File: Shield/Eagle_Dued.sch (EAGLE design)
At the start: 114 parts, among them IC1 7805TV, IC2 LM340MP-05, J10 Analog Inputs, J11 MOSFET OUTPUTS, J12 CANBUS, J8 DIGITAL INPUTS, X1 87758-1216

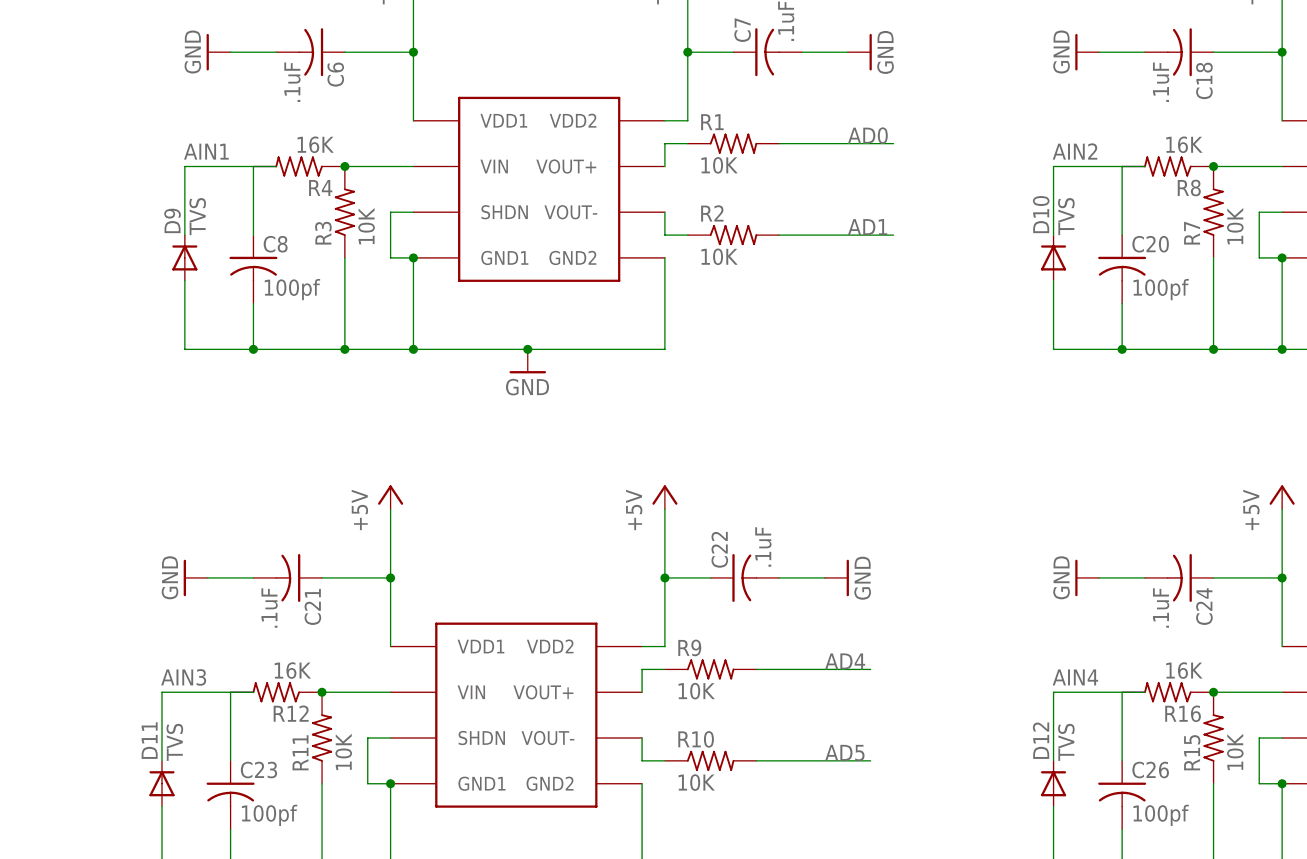
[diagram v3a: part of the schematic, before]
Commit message: Fixed a couple of errors in the schematic
Placed all parts on board approximately where they'll end up
(in theory)
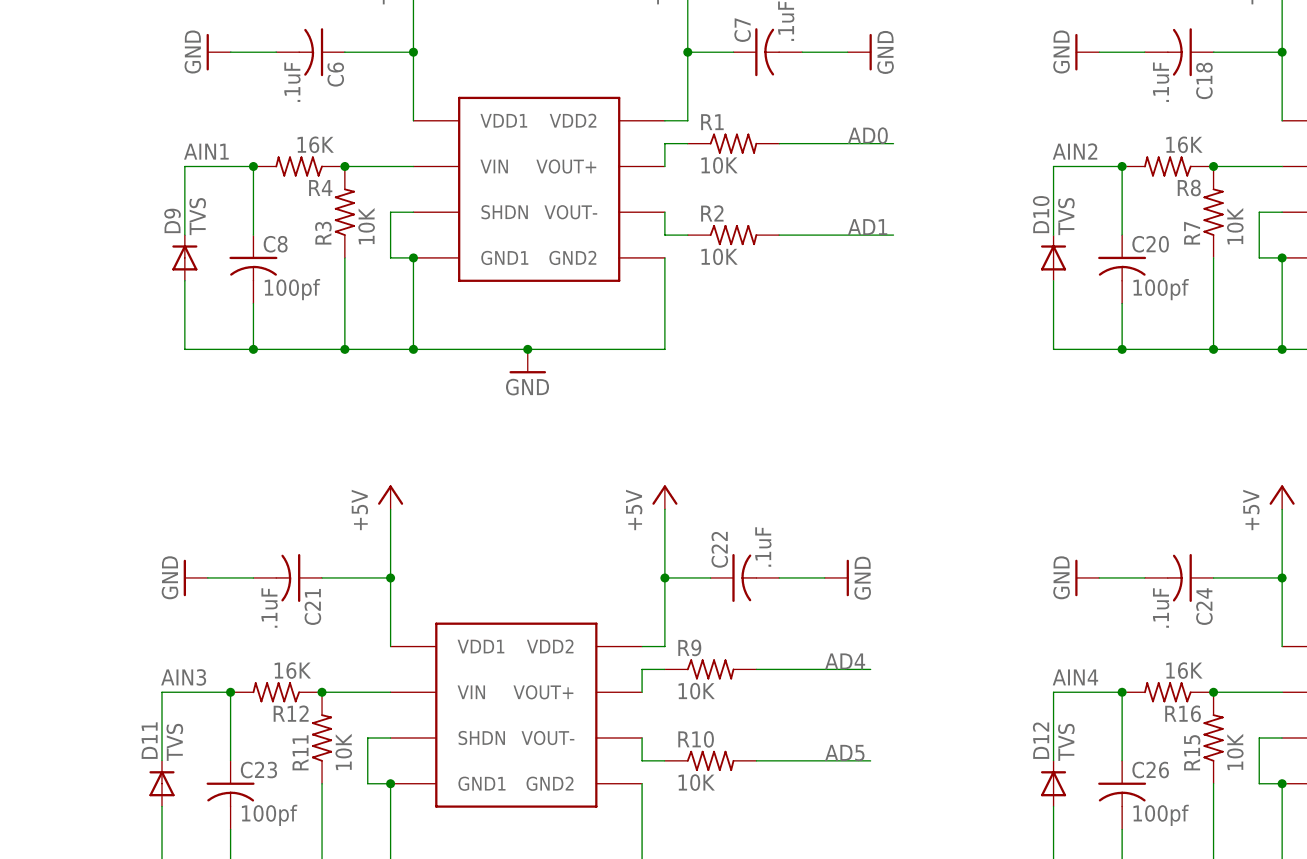
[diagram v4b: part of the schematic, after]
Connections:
- removed net N$14: C20.1, R8.2
- removed net N$18: C23.1, R12.2
- removed net N$22: C26.1, R16.2
- removed net N$9: C8.1, R4.2
- net AIN1: now also C8.1, R4.2
- net AIN2: now also C20.1, R8.2
- net AIN3: now also C23.1, R12.2
- net AIN4: now also C26.1, R16.2
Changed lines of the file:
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@@
 </segment>
 </net>
-<net name="N$9" class="0">
-<segment>
+<net name="AIN4" class="0">
+<segment>
+<pinref part="J10" gate="G$1" pin="4"/>
+<wire x1="398.78" y1="83.82" x2="411.48" y2="83.82" width="0.1524" layer="91"/>
+<label x="403.86" y="83.82" size="1.778" layer="95"/>
+</segment>
+<segment>
+<pinref part="D12" gate="G$1" pin="C"/>
+<wire x1="424.18" y1="-175.26" x2="424.18" y2="-182.88" width="0.1524" layer="91"/>
+<label x="429.26" y="-172.72" size="1.778" layer="95" rot="R180"/>
+<pinref part="R16" gate="G$1" pin="2"/>
+<pinref part="C26" gate="G$1" pin="1"/>
+<wire x1="431.8" y1="-175.26" x2="431.8" y2="-182.88" width="0.1524" layer="91"/>
+<wire x1="424.18" y1="-175.26" x2="431.8" y2="-175.26" width="0.1524" layer="91"/>
+<junction x="431.8" y="-175.26"/>
+</segment>
+</net>
+<net name="AIN3" class="0">
+<segment>
+<pinref part="J10" gate="G$1" pin="3"/>
+<wire x1="398.78" y1="81.28" x2="411.48" y2="81.28" width="0.1524" layer="91"/>
+<label x="403.86" y="81.28" size="1.778" layer="95"/>
+</segment>
+<segment>
+<pinref part="D11" gate="G$1" pin="C"/>
+<wire x1="325.12" y1="-175.26" x2="325.12" y2="-182.88" width="0.1524" layer="91"/>
+<label x="330.2" y="-172.72" size="1.778" layer="95" rot="R180"/>
+<pinref part="R12" gate="G$1" pin="2"/>
+<pinref part="C23" gate="G$1" pin="1"/>
+<wire x1="332.74" y1="-175.26" x2="332.74" y2="-182.88" width="0.1524" layer="91"/>
+<wire x1="325.12" y1="-175.26" x2="332.74" y2="-175.26" width="0.1524" layer="91"/>
+<junction x="332.74" y="-175.26"/>
+</segment>
+</net>
+<net name="AIN2" class="0">
+<segment>
+<pinref part="J10" gate="G$1" pin="2"/>
+<wire x1="398.78" y1="78.74" x2="411.48" y2="78.74" width="0.1524" layer="91"/>
+<label x="403.86" y="78.74" size="1.778" layer="95"/>
+</segment>
+<segment>
+<pinref part="D10" gate="G$1" pin="C"/>
+<wire x1="424.18" y1="-116.84" x2="424.18" y2="-124.46" width="0.1524" layer="91"/>
+<label x="429.26" y="-114.3" size="1.778" layer="95" rot="R180"/>
+<pinref part="R8" gate="G$1" pin="2"/>
+<pinref part="C20" gate="G$1" pin="1"/>
+<wire x1="431.8" y1="-116.84" x2="431.8" y2="-124.46" width="0.1524" layer="91"/>
+<wire x1="424.18" y1="-116.84" x2="431.8" y2="-116.84" width="0.1524" layer="91"/>
+<junction x="431.8" y="-116.84"/>
+</segment>
+</net>
+<net name="AIN1" class="0">
+<segment>
+<pinref part="J10" gate="G$1" pin="1"/>
+<wire x1="398.78" y1="76.2" x2="411.48" y2="76.2" width="0.1524" layer="91"/>
+<label x="403.86" y="76.2" size="1.778" layer="95"/>
+</segment>
+<segment>
+<pinref part="D9" gate="G$1" pin="C"/>
+<wire x1="327.66" y1="-116.84" x2="327.66" y2="-124.46" width="0.1524" layer="91"/>
+<label x="332.74" y="-114.3" size="1.778" layer="95" rot="R180"/>
 <pinref part="R4" gate="G$1" pin="2"/>
 <pinref part="C8" gate="G$1" pin="1"/>
 <wire x1="335.28" y1="-116.84" x2="335.28" y2="-124.46" width="0.1524" layer="91"/>
-</segment>
-</net>
-<net name="AIN4" class="0">
-<segment>
-<pinref part="J10" gate="G$1" pin="4"/>
-<wire x1="398.78" y1="83.82" x2="411.48" y2="83.82" width="0.1524" layer="91"/>
-<label x="403.86" y="83.82" size="1.778" layer="95"/>
-</segment>
-<segment>
-<wire x1="434.34" y1="-175.26" x2="424.18" y2="-175.26" width="0.1524" layer="91"/>
-<pinref part="D12" gate="G$1" pin="C"/>
-<wire x1="424.18" y1="-175.26" x2="424.18" y2="-182.88" width="0.1524" layer="91"/>
-<label x="429.26" y="-172.72" size="1.778" layer="95" rot="R180"/>
-</segment>
-</net>
-<net name="AIN3" class="0">
-<segment>
-<pinref part="J10" gate="G$1" pin="3"/>
-<wire x1="398.78" y1="81.28" x2="411.48" y2="81.28" width="0.1524" layer="91"/>
-<label x="403.86" y="81.28" size="1.778" layer="95"/>
-</segment>
-<segment>
-<wire x1="335.28" y1="-175.26" x2="325.12" y2="-175.26" width="0.1524" layer="91"/>
-<pinref part="D11" gate="G$1" pin="C"/>
-<wire x1="325.12" y1="-175.26" x2="325.12" y2="-182.88" width="0.1524" layer="91"/>
-<label x="330.2" y="-172.72" size="1.778" layer="95" rot="R180"/>
-</segment>
-</net>
-<net name="AIN2" class="0">
-<segment>
-<pinref part="J10" gate="G$1" pin="2"/>
-<wire x1="398.78" y1="78.74" x2="411.48" y2="78.74" width="0.1524" layer="91"/>
-<label x="403.86" y="78.74" size="1.778" layer="95"/>
-</segment>
-<segment>
-<wire x1="434.34" y1="-116.84" x2="424.18" y2="-116.84" width="0.1524" layer="91"/>
-<pinref part="D10" gate="G$1" pin="C"/>
-<wire x1="424.18" y1="-116.84" x2="424.18" y2="-124.46" width="0.1524" layer="91"/>
-<label x="429.26" y="-114.3" size="1.778" layer="95" rot="R180"/>
-</segment>
-</net>
-<net name="AIN1" class="0">
-<segment>
-<pinref part="J10" gate="G$1" pin="1"/>
-<wire x1="398.78" y1="76.2" x2="411.48" y2="76.2" width="0.1524" layer="91"/>
-<label x="403.86" y="76.2" size="1.778" layer="95"/>
-</segment>
-<segment>
-<wire x1="337.82" y1="-116.84" x2="327.66" y2="-116.84" width="0.1524" layer="91"/>
-<pinref part="D9" gate="G$1" pin="C"/>
-<wire x1="327.66" y1="-116.84" x2="327.66" y2="-124.46" width="0.1524" layer="91"/>
-<label x="332.74" y="-114.3" size="1.778" layer="95" rot="R180"/>
+<wire x1="327.66" y1="-116.84" x2="335.28" y2="-116.84" width="0.1524" layer="91"/>
+<junction x="335.28" y="-116.84"/>
 </segment>
 </net>
@@
 </segment>
 </net>
-<net name="N$14" class="0">
-<segment>
-<pinref part="R8" gate="G$1" pin="2"/>
-<pinref part="C20" gate="G$1" pin="1"/>
-<wire x1="431.8" y1="-116.84" x2="431.8" y2="-124.46" width="0.1524" layer="91"/>
-</segment>
-</net>
 <net name="N$15" class="0">
 <segment>
@@
 </segment>
 </net>
-<net name="N$18" class="0">
-<segment>
-<pinref part="R12" gate="G$1" pin="2"/>
-<pinref part="C23" gate="G$1" pin="1"/>
-<wire x1="332.74" y1="-175.26" x2="332.74" y2="-182.88" width="0.1524" layer="91"/>
-</segment>
-</net>
 <net name="N$19" class="0">
 <segment>
@@
 <wire x1="477.52" y1="-180.34" x2="477.52" y2="-182.88" width="0.1524" layer="91"/>
 <wire x1="477.52" y1="-182.88" x2="480.06" y2="-182.88" width="0.1524" layer="91"/>
-</segment>
-</net>
-<net name="N$22" class="0">
-<segment>
-<pinref part="R16" gate="G$1" pin="2"/>
-<pinref part="C26" gate="G$1" pin="1"/>
-<wire x1="431.8" y1="-175.26" x2="431.8" y2="-182.88" width="0.1524" layer="91"/>
 </segment>
 </net>
@@
 </sheet>
 </sheets>
-<errors>
-</errors>
 </schematic>
 </drawing>

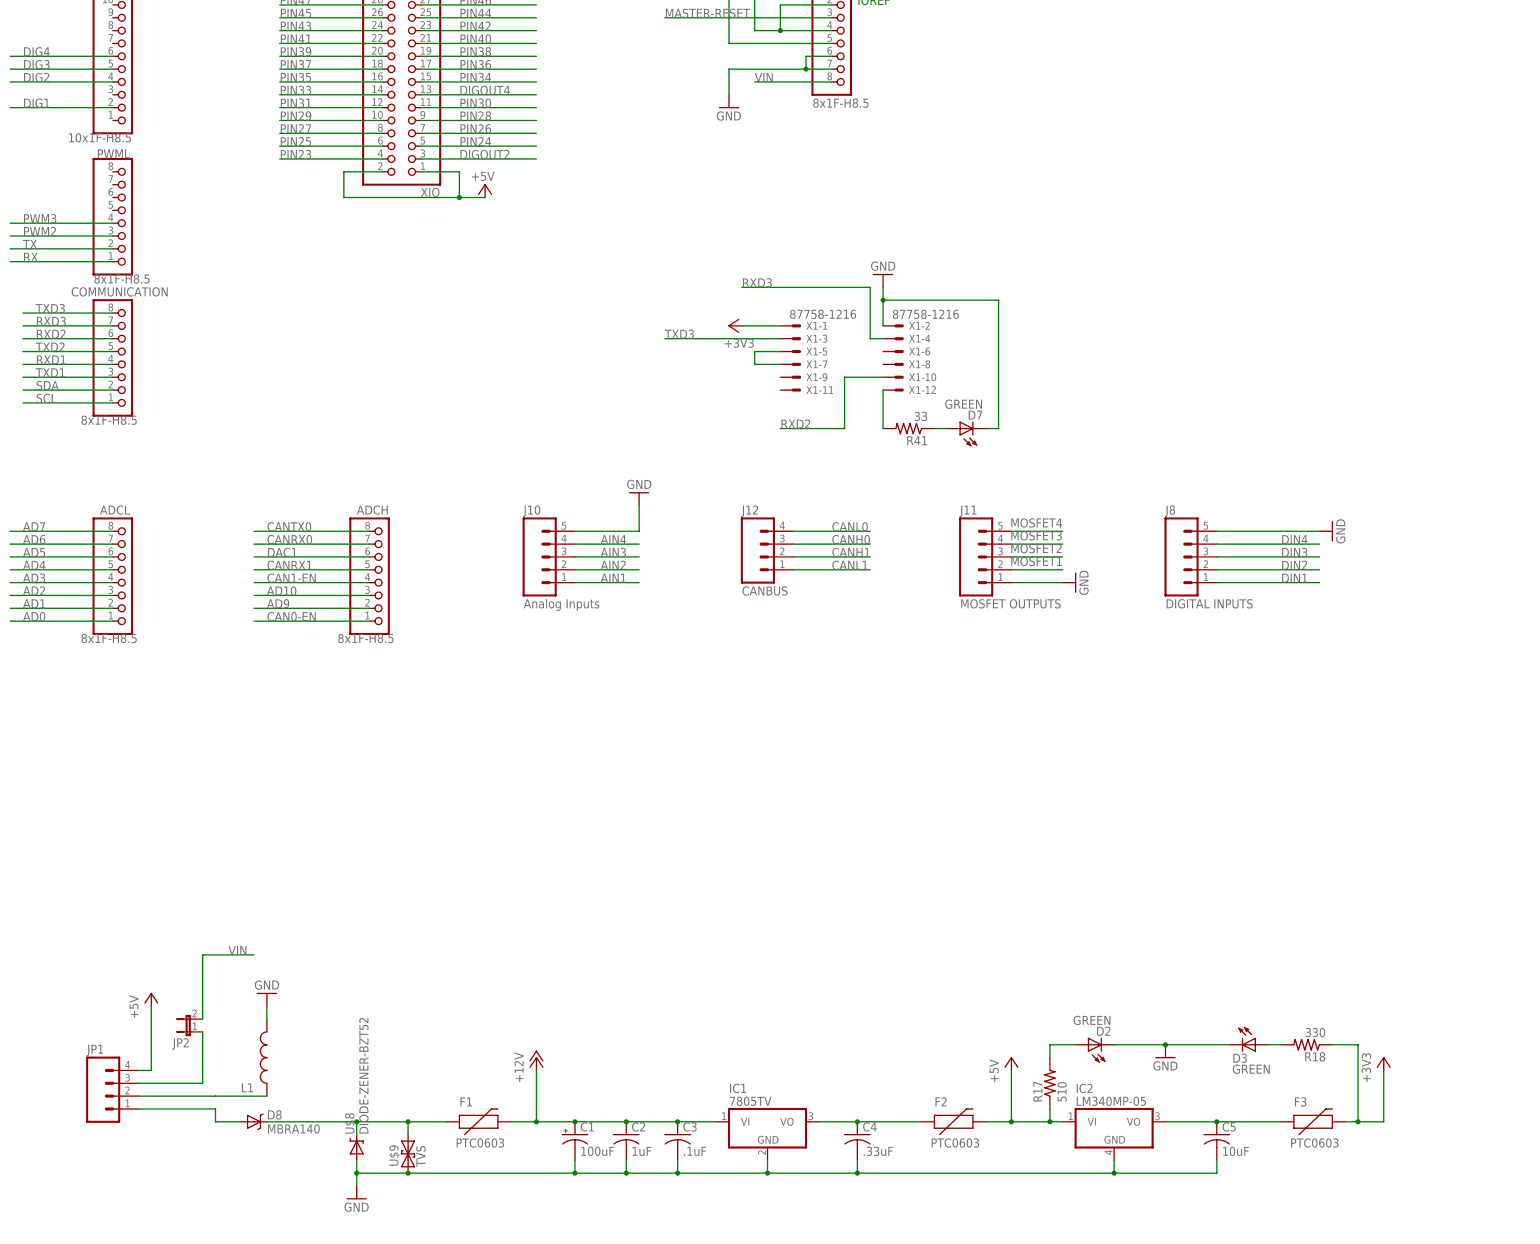
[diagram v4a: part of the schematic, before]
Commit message: Slight component move on canbus Shield, drastic change to DueD to use ampseal and wifi layout
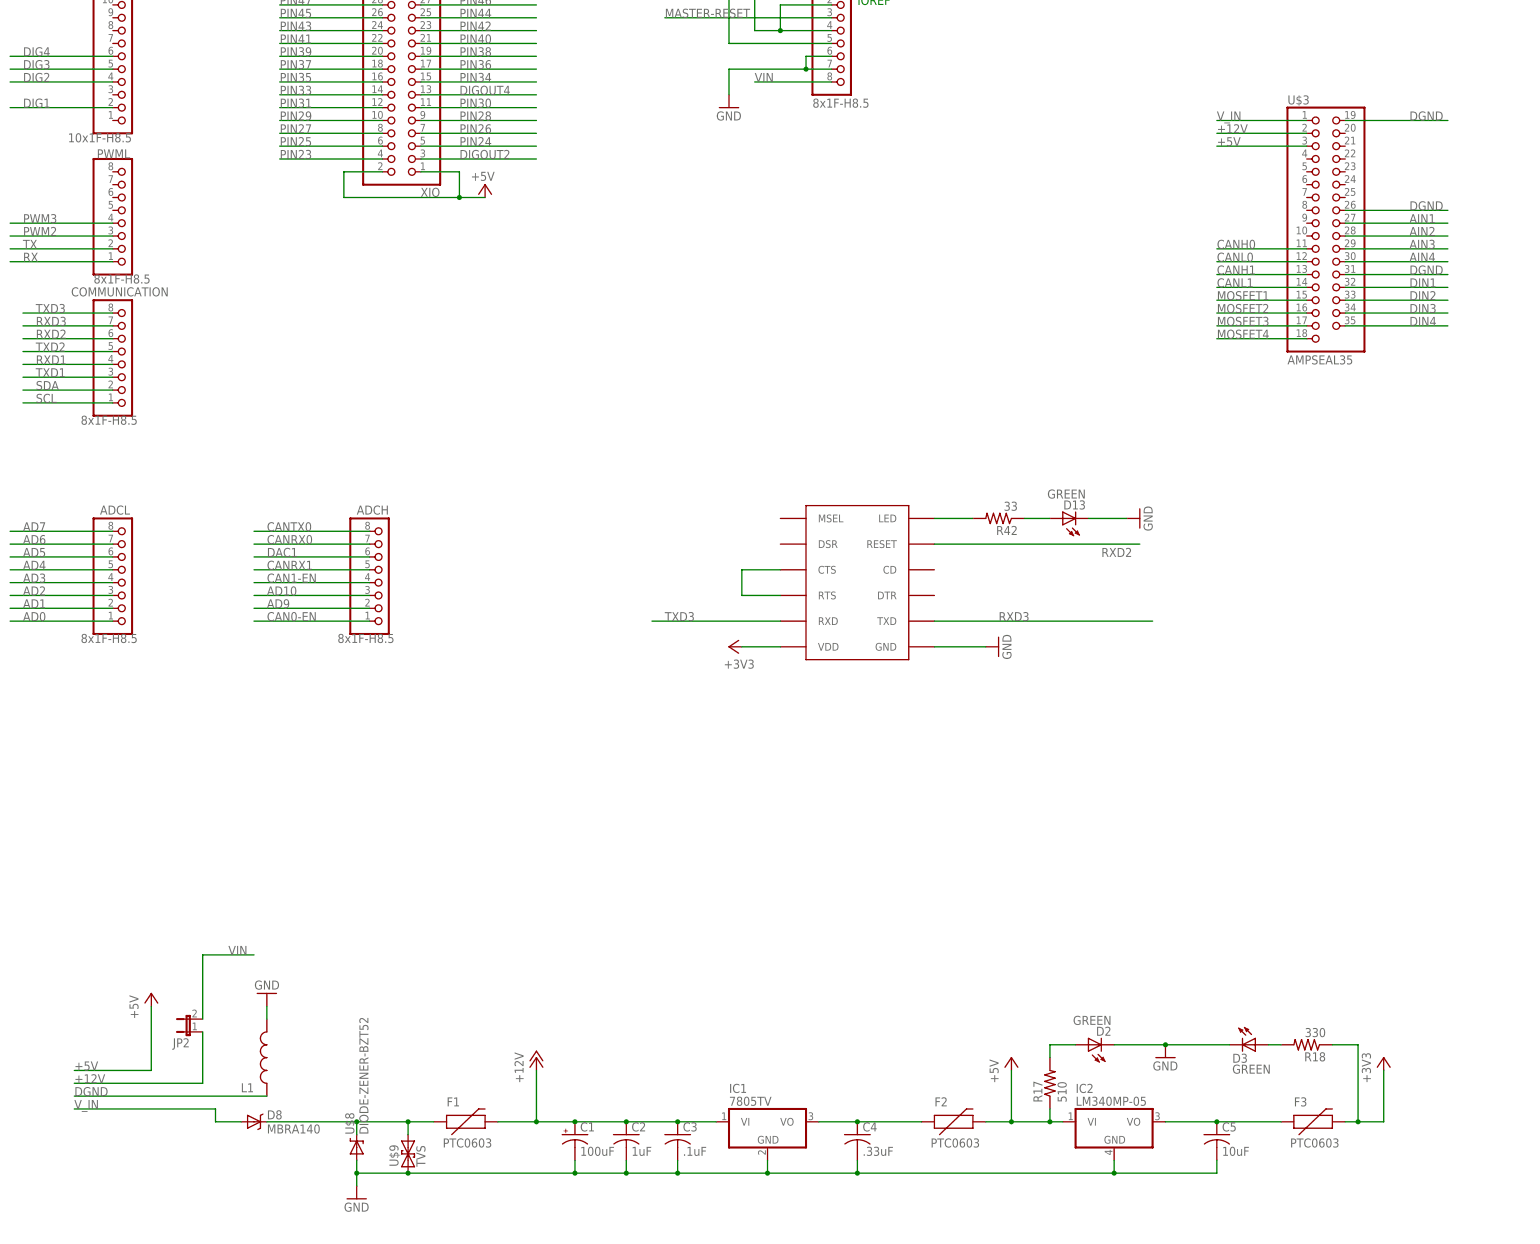
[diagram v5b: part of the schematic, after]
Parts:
- removed D7: GREEN, SparkFun-LED:LED-GREEN0603
- removed J10: Analog Inputs, SparkFun-Connectors:M05PTH
- removed J11: MOSFET OUTPUTS, SparkFun-Connectors:M05PTH
- removed J12: CANBUS, SparkFun-Connectors:M04PTH
- removed J8: DIGITAL INPUTS, SparkFun-Connectors:M05PTH
- removed JP1: (no value), SparkFun-Connectors:M04PTH
- removed R41: 33, rcl:R-US_R0603
- removed X1: 87758-1216, con-molex:87758-1216
- added D13: GREEN, SparkFun-LED:LED-GREEN0603
- added R42: 33, rcl:R-US_R0603
- added U$3: AMPSEAL35, Ampseal:AMPSEAL35
- added U$4: MINIWIFI, ck_custom:MINIWIFI
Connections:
- removed net N$1: JP1.2, L1.1
- removed net N$35: X1-5.S, X1-7.S
- removed net N$37: D7.A, R41.1
- removed net N$39: R41.2, X1-12.S
- new net DGND: L1.1, U$3.19, U$3.26, U$3.31
- new net N$9: D13.A, R42.1
- new net V_IN: D8.A, U$3.1
- net +12V: now also JP2.1, U$3.2
- net +3V3: now also U$4.VDD; no longer X1-1.S
- net +5V: now also U$3.3; no longer JP1.4
- net AIN1: now also U$3.27; no longer J10.1
- net AIN2: now also U$3.28; no longer J10.2
- net AIN3: now also U$3.29; no longer J10.3
- net AIN4: now also U$3.30; no longer J10.4
- net CANH0: now also U$3.11; no longer J12.3
- net CANH1: now also U$3.13; no longer J12.2
- net CANL0: now also U$3.12; no longer J12.4
- net CANL1: now also U$3.14; no longer J12.1
- net DIN1: now also U$3.32; no longer J8.1
- net DIN2: now also U$3.33; no longer J8.2
- net DIN3: now also U$3.34; no longer J8.3
- net DIN4: now also U$3.35; no longer J8.4
- net GND: now also D13.C, U$4.GND; no longer D7.C, J10.5, J11.1, J8.5, X1-2.S
- net MOSFET1: now also U$3.15; no longer J11.2
- net MOSFET2: now also U$3.16; no longer J11.3
- net MOSFET3: now also U$3.17; no longer J11.4
- net MOSFET4: now also U$3.18; no longer J11.5
- net N$2: now also U$4.CTS, U$4.RTS; no longer D8.A, JP1.1
- net N$4: now also R42.2, U$4.LED; no longer JP1.3, JP2.1
- net RXD2: now also U$4.RESET; no longer X1-10.S
- net RXD3: now also U$4.TXD; no longer X1-4.S
- net TXD3: now also U$4.RXD; no longer X1-3.S
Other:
- moved on the sheet: F1
